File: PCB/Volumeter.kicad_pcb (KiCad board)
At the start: 2 copper layers, 50.8 x 15.2 mm, 12 parts, among them SW1 SW_Push, U1 ATtiny85-20PU

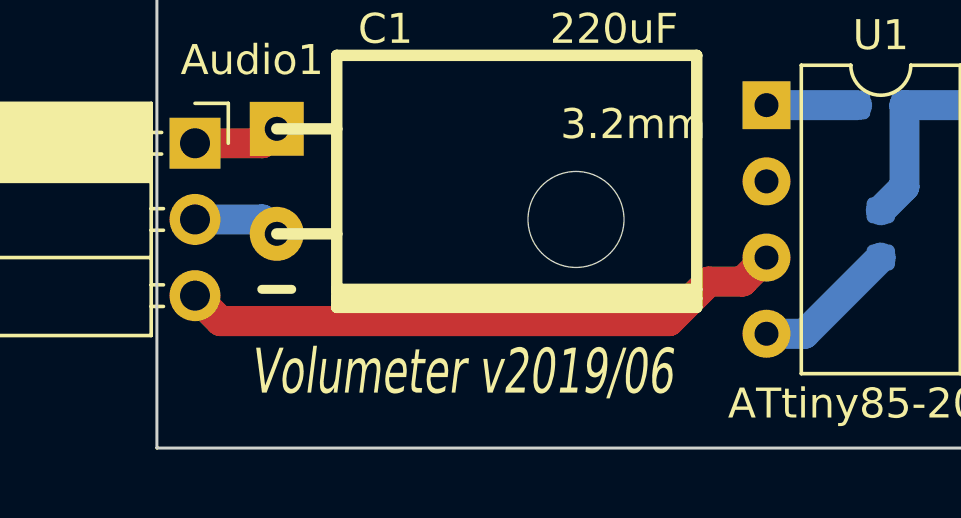
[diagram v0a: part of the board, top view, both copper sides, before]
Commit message: increase hole clearance
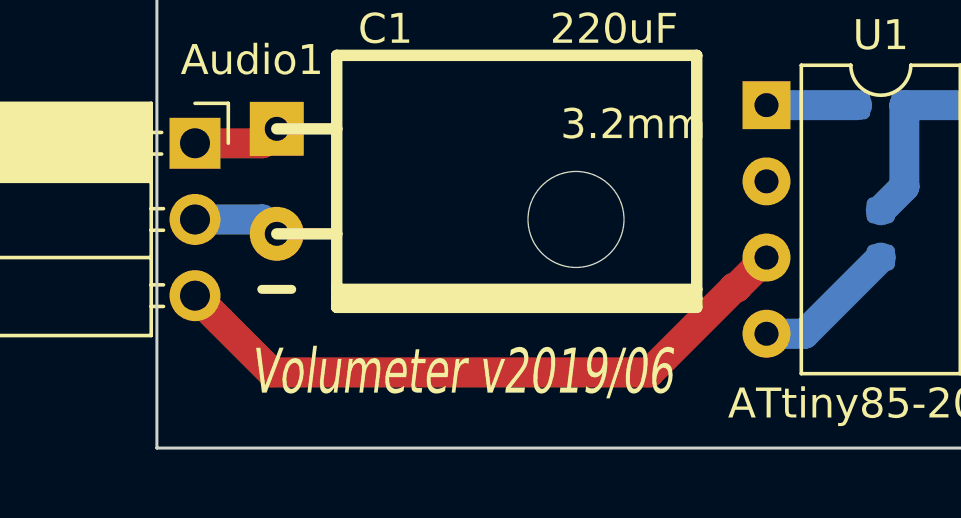
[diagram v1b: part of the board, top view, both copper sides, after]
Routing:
- net /audio: track 20.3 -> 21.7 mm
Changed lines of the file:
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@@
     (thickness 1.6)
     (drawings 11)
-    (tracks 31)
+    (tracks 32)
     (zones 0)
     (modules 12)
@@
   )
   (setup
-    (last_trace_width 1)
+    (last_trace_width 2)
     (user_trace_width 0.5)
     (user_trace_width 1)
@@
     (mod_text_size 1 1)
     (mod_text_width 0.15)
-    (pad_size 1.25 1.75)
-    (pad_drill 0)
+    (pad_size 3.2 3.2)
+    (pad_drill 3.2)
     (pad_to_mask_clearance 0.051)
     (solder_mask_min_width 0.25)
@@
     (descr "Mounting Hole 3.2mm, no annular, M3, ISO14580")
     (tags "mounting hole 3.2mm no annular m3 iso14580")
-    (clearance 1)
+    (clearance 3)
     (attr virtual)
     (fp_text reference H1 (at 0 -3.75) (layer F.SilkS) hide
@@
     (fp_circle (center 0 0) (end 2.75 0) (layer Cmts.User) (width 0.15))
     (fp_circle (center 0 0) (end 3 0) (layer F.CrtYd) (width 0.05))
-    (pad 1 np_thru_hole circle (at 0 0) (size 3.2 3.2) (drill 3.2) (layers *.Cu *.Mask))
+    (pad "" np_thru_hole circle (at 0 0) (size 3.2 3.2) (drill 3.2) (layers *.Cu *.Mask))
   )
   (module Fuse:Fuse_1206_3216Metric (layer F.Cu)
@@
   (segment (start 64.64 34.42) (end 66.04 33.02) (width 2) (layer F.Cu) (net 7))
   (segment (start 64.64 36.83) (end 64.64 34.42) (width 2) (layer F.Cu) (net 7))
-  (segment (start 42.380001 33.819999) (end 43.18 33.02) (width 1) (layer F.Cu) (net 8))
-  (segment (start 41.254231 33.819999) (end 42.380001 33.819999) (width 1) (layer F.Cu) (net 8))
-  (segment (start 39.934231 35.139999) (end 41.254231 33.819999) (width 1) (layer F.Cu) (net 8))
-  (segment (start 24.979999 35.139999) (end 39.934231 35.139999) (width 1) (layer F.Cu) (net 8))
-  (segment (start 24.13 34.29) (end 24.979999 35.139999) (width 1) (layer F.Cu) (net 8))
+  (segment (start 24.979999 35.139999) (end 24.13 34.29) (width 1) (layer F.Cu) (net 8))
+  (segment (start 26.690001 36.850001) (end 24.979999 35.139999) (width 1) (layer F.Cu) (net 8))
+  (segment (start 39.278001 36.850001) (end 26.690001 36.850001) (width 1) (layer F.Cu) (net 8))
+  (segment (start 42.107992 34.02001) (end 39.278001 36.850001) (width 1) (layer F.Cu) (net 8))
+  (segment (start 42.17999 34.02001) (end 42.107992 34.02001) (width 1) (layer F.Cu) (net 8))
+  (segment (start 43.18 33.02) (end 42.17999 34.02001) (width 1) (layer F.Cu) (net 8))
   (zone (net 0) (net_name "") (layer F.Cu) (hatch full 0.508)
     (connect_pads (clearance 0.508))
